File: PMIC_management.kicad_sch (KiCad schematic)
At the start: 25 parts, among them SW1 SW_Push, SW2 SW_Push, U3 RK809-2, Y2 32.768Khz

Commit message: updated Reference, and PCB
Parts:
- BT1: footprint (none) -> TestPoint:TestPoint_2Pads_Pitch5.08mm_Drill1.3mm
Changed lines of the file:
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@@
       (effects (font (size 1.27 1.27)) (justify left))
     )
-    (property "Footprint" "" (at 237.49 44.196 90)
+    (property "Footprint" "TestPoint:TestPoint_2Pads_Pitch5.08mm_Drill1.3mm" (at 237.49 44.196 90)
       (effects (font (size 1.27 1.27)) hide)
     )

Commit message: updated LCSC selection of capacitors
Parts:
- C43, C49: value 100nF X5R 16V -> 100nF X5R 6.3V; footprint Capacitor_SMD:C_0402_1005Metric -> Capacitor_SMD:C_0201_0603Metric; LCSC (none) -> C76934; Model (none) -> GRM033R61A104KE15D; Vendor (none) -> muRata(村田)
- C44, C45: value 22uF 50V C0G -> 22pF 50V C0G; footprint Capacitor_SMD:C_0402_1005Metric -> Capacitor_SMD:C_0201_0603Metric; LCSC (none) -> C76924; Model (none) -> GRM0335C1H220JA01D; Vendor (none) -> muRata(村田)
- C46, C47: value 1uF 10V X5R -> 1uF X5R 6.3V; footprint Capacitor_SMD:C_0402_1005Metric -> Capacitor_SMD:C_0201_0603Metric; LCSC (none) -> C76929; Model (none) -> GRM033R60J105KEA2D; Vendor (none) -> muRata(村田)
- C48: footprint (none) -> Capacitor_SMD:C_0603_1608Metric
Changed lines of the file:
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@@
       (effects (font (size 1.27 1.27)))
     )
-    (property "Value" "22uF 50V C0G" (at 74.93 76.2 90)
-      (effects (font (size 1.27 1.27)))
-    )
-    (property "Footprint" "Capacitor_SMD:C_0402_1005Metric" (at 69.85 73.9648 0)
+    (property "Value" "22pF 50V C0G" (at 74.93 76.2 90)
+      (effects (font (size 1.27 1.27)))
+    )
+    (property "Footprint" "Capacitor_SMD:C_0201_0603Metric" (at 69.85 73.9648 0)
       (effects (font (size 1.27 1.27)) hide)
     )
     (property "Datasheet" "~" (at 66.04 74.93 0)
+      (effects (font (size 1.27 1.27)) hide)
+    )
+    (property "Description" "容值: 22pF 精度: ±5% 额定电压: 50V 材质(温度系数): C0G 材质:C0G" (at 66.04 74.93 0)
+      (effects (font (size 1.27 1.27)) hide)
+    )
+    (property "LCSC" "C76924" (at 66.04 74.93 0)
+      (effects (font (size 1.27 1.27)) hide)
+    )
+    (property "Model" "GRM0335C1H220JA01D" (at 66.04 74.93 0)
+      (effects (font (size 1.27 1.27)) hide)
+    )
+    (property "Vendor" "muRata(村田)" (at 66.04 74.93 0)
       (effects (font (size 1.27 1.27)) hide)
     )
@@
       (effects (font (size 1.27 1.27)))
     )
-    (property "Value" "22uF 50V C0G" (at 74.93 66.04 90)
-      (effects (font (size 1.27 1.27)))
-    )
-    (property "Footprint" "Capacitor_SMD:C_0402_1005Metric" (at 69.85 66.3448 0)
+    (property "Value" "22pF 50V C0G" (at 74.93 66.04 90)
+      (effects (font (size 1.27 1.27)))
+    )
+    (property "Footprint" "Capacitor_SMD:C_0201_0603Metric" (at 69.85 66.3448 0)
       (effects (font (size 1.27 1.27)) hide)
     )
     (property "Datasheet" "~" (at 66.04 67.31 0)
+      (effects (font (size 1.27 1.27)) hide)
+    )
+    (property "Description" "容值: 22pF 精度: ±5% 额定电压: 50V 材质(温度系数): C0G 材质:C0G" (at 66.04 67.31 0)
+      (effects (font (size 1.27 1.27)) hide)
+    )
+    (property "LCSC" "C76924" (at 66.04 67.31 0)
+      (effects (font (size 1.27 1.27)) hide)
+    )
+    (property "Model" "GRM0335C1H220JA01D" (at 66.04 67.31 0)
+      (effects (font (size 1.27 1.27)) hide)
+    )
+    (property "Vendor" "muRata(村田)" (at 66.04 67.31 0)
       (effects (font (size 1.27 1.27)) hide)
     )
@@
       (effects (font (size 1.27 1.27)) (justify left))
     )
-    (property "Value" "100nF X5R 16V" (at 36.83 130.81 0)
-      (effects (font (size 1.27 1.27)) (justify left))
-    )
-    (property "Footprint" "Capacitor_SMD:C_0402_1005Metric" (at 53.0352 130.81 0)
+    (property "Value" "100nF X5R 6.3V" (at 36.83 130.81 0)
+      (effects (font (size 1.27 1.27)) (justify left))
+    )
+    (property "Footprint" "Capacitor_SMD:C_0201_0603Metric" (at 53.0352 130.81 0)
       (effects (font (size 1.27 1.27)) hide)
     )
@@
       (effects (font (size 1.27 1.27)) hide)
     )
+    (property "Description" "容值: 100nF 精度: ±10% 额定电压: 10V 材质(温度系数): X5R 材质:X5R" (at 52.07 127 0)
+      (effects (font (size 1.27 1.27)) hide)
+    )
+    (property "Model" "GRM033R61A104KE15D" (at 52.07 127 0)
+      (effects (font (size 1.27 1.27)) hide)
+    )
+    (property "Vendor" "muRata(村田)" (at 52.07 127 0)
+      (effects (font (size 1.27 1.27)) hide)
+    )
+    (property "LCSC" "C76934" (at 52.07 127 0)
+      (effects (font (size 1.27 1.27)) hide)
+    )
     (pin "1")
     (pin "2")
@@
       (effects (font (size 1.27 1.27)))
     )
-    (property "Value" "1uF 10V X5R" (at 168.91 51.3621 90)
-      (effects (font (size 1.27 1.27)))
-    )
-    (property "Footprint" "Capacitor_SMD:C_0402_1005Metric" (at 172.72 53.6448 0)
+    (property "Value" "1uF X5R 6.3V" (at 168.91 51.3621 90)
+      (effects (font (size 1.27 1.27)))
+    )
+    (property "Footprint" "Capacitor_SMD:C_0201_0603Metric" (at 172.72 53.6448 0)
       (effects (font (size 1.27 1.27)) hide)
     )
@@
       (effects (font (size 1.27 1.27)) hide)
     )
+    (property "Description" "容值: 1uF 精度: ±10% 额定电压: 6.3V 材质(温度系数): X5R 材质:X5R" (at 168.91 54.61 0)
+      (effects (font (size 1.27 1.27)) hide)
+    )
+    (property "LCSC" "C76929" (at 168.91 54.61 0)
+      (effects (font (size 1.27 1.27)) hide)
+    )
+    (property "Model" "GRM033R60J105KEA2D" (at 168.91 54.61 0)
+      (effects (font (size 1.27 1.27)) hide)
+    )
+    (property "Vendor" "muRata(村田)" (at 168.91 54.61 0)
+      (effects (font (size 1.27 1.27)) hide)
+    )
     (pin "1")
     (pin "2")
@@
       (effects (font (size 1.27 1.27)) (justify left))
     )
-    (property "Footprint" "" (at 178.7652 107.95 0)
+    (property "Footprint" "Capacitor_SMD:C_0603_1608Metric" (at 178.7652 107.95 0)
       (effects (font (size 1.27 1.27)) hide)
     )
@@
       (effects (font (size 1.27 1.27)) (justify right))
     )
-    (property "Value" "100nF X5R 16V" (at 238.76 132.08 90)
-      (effects (font (size 1.27 1.27)) (justify right))
-    )
-    (property "Footprint" "Capacitor_SMD:C_0402_1005Metric" (at 240.03 133.6548 0)
+    (property "Value" "100nF X5R 6.3V" (at 238.76 132.08 90)
+      (effects (font (size 1.27 1.27)) (justify right))
+    )
+    (property "Footprint" "Capacitor_SMD:C_0201_0603Metric" (at 240.03 133.6548 0)
       (effects (font (size 1.27 1.27)) hide)
     )
@@
       (effects (font (size 1.27 1.27)) hide)
     )
+    (property "Description" "容值: 100nF 精度: ±10% 额定电压: 10V 材质(温度系数): X5R 材质:X5R" (at 236.22 134.62 0)
+      (effects (font (size 1.27 1.27)) hide)
+    )
+    (property "Model" "GRM033R61A104KE15D" (at 236.22 134.62 0)
+      (effects (font (size 1.27 1.27)) hide)
+    )
+    (property "Vendor" "muRata(村田)" (at 236.22 134.62 0)
+      (effects (font (size 1.27 1.27)) hide)
+    )
+    (property "LCSC" "C76934" (at 236.22 134.62 0)
+      (effects (font (size 1.27 1.27)) hide)
+    )
     (pin "1")
     (pin "2")
@@
       (effects (font (size 1.27 1.27)))
     )
-    (property "Value" "1uF 10V X5R" (at 86.36 52.07 90)
-      (effects (font (size 1.27 1.27)))
-    )
-    (property "Footprint" "Capacitor_SMD:C_0402_1005Metric" (at 82.55 52.3748 0)
+    (property "Value" "1uF X5R 6.3V" (at 86.36 52.07 90)
+      (effects (font (size 1.27 1.27)))
+    )
+    (property "Footprint" "Capacitor_SMD:C_0201_0603Metric" (at 82.55 52.3748 0)
       (effects (font (size 1.27 1.27)) hide)
     )
@@
       (effects (font (size 1.27 1.27)) hide)
     )
+    (property "Description" "容值: 1uF 精度: ±10% 额定电压: 6.3V 材质(温度系数): X5R 材质:X5R" (at 78.74 53.34 0)
+      (effects (font (size 1.27 1.27)) hide)
+    )
+    (property "LCSC" "C76929" (at 78.74 53.34 0)
+      (effects (font (size 1.27 1.27)) hide)
+    )
+    (property "Model" "GRM033R60J105KEA2D" (at 78.74 53.34 0)
+      (effects (font (size 1.27 1.27)) hide)
+    )
+    (property "Vendor" "muRata(村田)" (at 78.74 53.34 0)
+      (effects (font (size 1.27 1.27)) hide)
+    )

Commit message: updated foorprints
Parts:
- D13: value ESD545IN -> ESD 3.3V; footprint Diode_SMD:D_0402_1005Metric -> Diode_SMD:Nexperia_DSN0603-2_0.6x0.3mm_P0.4mm; LCSC (none) -> C172400; Model (none) -> LESD11D3.3CT5G; Vendor (none) -> LRC(乐山无线电)
- D14, D15: value ESD545IN -> ESD 5.0V; footprint Diode_SMD:D_0402_1005Metric -> Diode_SMD:Nexperia_DSN0603-2_0.6x0.3mm_P0.4mm; LCSC (none) -> C172403; Model (none) -> LESD11LL5.0CT5G; Vendor (none) -> LRC(乐山无线电)
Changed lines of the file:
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@@
     (stroke (width 0) (type default))
+  )
+  (text_box "PWR_ON: Power on key input, active low, internal 17k resistor pull high\nto VCC_RTC"
+    (at 134.62 120.65 0) (size 38.1 8.89)
+    (stroke (width 0) (type dash_dot) (color 194 194 0 1))
+    (fill (type none))
+    (effects (font (size 1.27 1.27) (color 194 194 0 1)) (justify left top))
   )
   (text "还需要考虑充电/保护电路" (at 210.82 22.86 0)
@@
       (effects (font (size 1.27 1.27)) (justify right))
     )
-    (property "Value" "ESD545IN" (at 237.49 121.92 0)
-      (effects (font (size 1.27 1.27)) (justify right))
-    )
-    (property "Footprint" "Diode_SMD:D_0402_1005Metric" (at 236.22 124.46 0)
-      (effects (font (size 1.27 1.27)) hide)
-    )
-    (property "Datasheet" "https://www.onsemi.com/pub/Collateral/ESD9B-D.PDF" (at 236.22 124.46 0)
+    (property "Value" "ESD 5.0V" (at 237.49 121.92 0)
+      (effects (font (size 1.27 1.27)) (justify right))
+    )
+    (property "Footprint" "Diode_SMD:Nexperia_DSN0603-2_0.6x0.3mm_P0.4mm" (at 236.22 124.46 0)
+      (effects (font (size 1.27 1.27)) hide)
+    )
+    (property "Datasheet" "" (at 236.22 124.46 0)
+      (effects (font (size 1.27 1.27)) hide)
+    )
+    (property "Description" "极性: 双向 反向截止电压(Vrwm): 5V 击穿电压(VBR): 6V 峰值脉冲电流(Ipp)@8/20us: 4A 钳位电压(Vc)@Ipp: 20V" (at 236.22 124.46 0)
+      (effects (font (size 1.27 1.27)) hide)
+    )
+    (property "LCSC" "C172403" (at 236.22 124.46 0)
+      (effects (font (size 1.27 1.27)) hide)
+    )
+    (property "Model" "LESD11LL5.0CT5G" (at 236.22 124.46 0)
+      (effects (font (size 1.27 1.27)) hide)
+    )
+    (property "Vendor" "LRC(乐山无线电)" (at 236.22 124.46 0)
       (effects (font (size 1.27 1.27)) hide)
     )
@@
       (effects (font (size 1.27 1.27)) (justify right))
     )
-    (property "Value" "ESD545IN" (at 267.97 44.45 90)
-      (effects (font (size 1.27 1.27)) (justify right))
-    )
-    (property "Footprint" "Diode_SMD:D_0402_1005Metric" (at 265.43 43.18 0)
-      (effects (font (size 1.27 1.27)) hide)
-    )
-    (property "Datasheet" "https://www.onsemi.com/pub/Collateral/ESD9B-D.PDF" (at 265.43 43.18 0)
+    (property "Value" "ESD 5.0V" (at 267.97 44.45 90)
+      (effects (font (size 1.27 1.27)) (justify right))
+    )
+    (property "Footprint" "Diode_SMD:Nexperia_DSN0603-2_0.6x0.3mm_P0.4mm" (at 265.43 43.18 0)
+      (effects (font (size 1.27 1.27)) hide)
+    )
+    (property "Datasheet" "" (at 265.43 43.18 0)
+      (effects (font (size 1.27 1.27)) hide)
+    )
+    (property "Description" "极性: 双向 反向截止电压(Vrwm): 5V 击穿电压(VBR): 6V 峰值脉冲电流(Ipp)@8/20us: 4A 钳位电压(Vc)@Ipp: 20V" (at 265.43 43.18 0)
+      (effects (font (size 1.27 1.27)) hide)
+    )
+    (property "LCSC" "C172403" (at 265.43 43.18 0)
+      (effects (font (size 1.27 1.27)) hide)
+    )
+    (property "Model" "LESD11LL5.0CT5G" (at 265.43 43.18 0)
+      (effects (font (size 1.27 1.27)) hide)
+    )
+    (property "Vendor" "LRC(乐山无线电)" (at 265.43 43.18 0)
       (effects (font (size 1.27 1.27)) hide)
     )
@@
       (effects (font (size 1.27 1.27)) (justify right))
     )
-    (property "Value" "ESD545IN" (at 69.85 128.27 90)
-      (effects (font (size 1.27 1.27)) (justify right))
-    )
-    (property "Footprint" "Diode_SMD:D_0402_1005Metric" (at 67.31 127 0)
-      (effects (font (size 1.27 1.27)) hide)
-    )
-    (property "Datasheet" "https://www.onsemi.com/pub/Collateral/ESD9B-D.PDF" (at 67.31 127 0)
-      (effects (font (size 1.27 1.27)) hide)
-    )
+    (property "Value" "ESD 3.3V" (at 69.85 128.27 90)
+      (effects (font (size 1.27 1.27)) (justify right))
+    )
+    (property "Footprint" "Diode_SMD:Nexperia_DSN0603-2_0.6x0.3mm_P0.4mm" (at 67.31 127 0)
+      (effects (font (size 1.27 1.27)) hide)
+    )
+    (property "Datasheet" "" (at 67.31 127 0)
+      (effects (font (size 1.27 1.27)) hide)
+    )
+    (property "Description" "极性: 双向 反向截止电压(Vrwm): 3.3V 击穿电压(VBR): 5V 峰值脉冲电流(Ipp)@8/20us: 6A 钳位电压" (at 67.31 127 0)
+      (effects (font (size 1.27 1.27)) hide)
+    )
+    (property "LCSC" "C172400" (at 67.31 127 0)
+      (effects (font (size 1.27 1.27)) hide)
+    )
+    (property "Model" "LESD11D3.3CT5G" (at 67.31 127 0)
+      (effects (font (size 1.27 1.27)) hide)
+    )
+    (property "Vendor" "LRC(乐山无线电)" (at 67.31 127 0)
+      (effects (font (size 1.27 1.27)) hide)
+    )

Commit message: layout SoC Power and DDR capacitors
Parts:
- C43, C49: LCSC C76934 -> C76928; Model GRM033R61A104KE15D -> GRM033R60J104KE19D
- C46, C47: footprint Capacitor_SMD:C_0201_0603Metric -> Capacitor_SMD:C_0402_1005Metric; LCSC C76929 -> C15684; Model GRM033R60J105KEA2D -> GRM155R60J105KE19D
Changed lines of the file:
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@@
       (effects (font (size 1.27 1.27)) hide)
     )
-    (property "Description" "容值: 100nF 精度: ±10% 额定电压: 10V 材质(温度系数): X5R 材质:X5R" (at 52.07 127 0)
-      (effects (font (size 1.27 1.27)) hide)
-    )
-    (property "Model" "GRM033R61A104KE15D" (at 52.07 127 0)
+    (property "Description" "容值: 100nF 精度: ±10% 额定电压: 6.3V 材质(温度系数): X5R 材质:X5R" (at 52.07 127 0)
+      (effects (font (size 1.27 1.27)) hide)
+    )
+    (property "Model" "GRM033R60J104KE19D" (at 52.07 127 0)
       (effects (font (size 1.27 1.27)) hide)
     )
@@
       (effects (font (size 1.27 1.27)) hide)
     )
-    (property "LCSC" "C76934" (at 52.07 127 0)
+    (property "LCSC" "C76928" (at 52.07 127 0)
       (effects (font (size 1.27 1.27)) hide)
     )
@@
       (effects (font (size 1.27 1.27)))
     )
-    (property "Footprint" "Capacitor_SMD:C_0201_0603Metric" (at 172.72 53.6448 0)
+    (property "Footprint" "Capacitor_SMD:C_0402_1005Metric" (at 172.72 53.6448 0)
       (effects (font (size 1.27 1.27)) hide)
     )
@@
       (effects (font (size 1.27 1.27)) hide)
     )
-    (property "LCSC" "C76929" (at 168.91 54.61 0)
-      (effects (font (size 1.27 1.27)) hide)
-    )
-    (property "Model" "GRM033R60J105KEA2D" (at 168.91 54.61 0)
+    (property "LCSC" "C15684" (at 168.91 54.61 0)
+      (effects (font (size 1.27 1.27)) hide)
+    )
+    (property "Model" "GRM155R60J105KE19D" (at 168.91 54.61 0)
       (effects (font (size 1.27 1.27)) hide)
     )
@@
       (effects (font (size 1.27 1.27)) hide)
     )
-    (property "Description" "容值: 100nF 精度: ±10% 额定电压: 10V 材质(温度系数): X5R 材质:X5R" (at 236.22 134.62 0)
-      (effects (font (size 1.27 1.27)) hide)
-    )
-    (property "Model" "GRM033R61A104KE15D" (at 236.22 134.62 0)
+    (property "Description" "容值: 100nF 精度: ±10% 额定电压: 6.3V 材质(温度系数): X5R 材质:X5R" (at 236.22 134.62 0)
+      (effects (font (size 1.27 1.27)) hide)
+    )
+    (property "Model" "GRM033R60J104KE19D" (at 236.22 134.62 0)
       (effects (font (size 1.27 1.27)) hide)
     )
@@
       (effects (font (size 1.27 1.27)) hide)
     )
-    (property "LCSC" "C76934" (at 236.22 134.62 0)
+    (property "LCSC" "C76928" (at 236.22 134.62 0)
       (effects (font (size 1.27 1.27)) hide)
     )
@@
       (effects (font (size 1.27 1.27)))
     )
-    (property "Footprint" "Capacitor_SMD:C_0201_0603Metric" (at 82.55 52.3748 0)
+    (property "Footprint" "Capacitor_SMD:C_0402_1005Metric" (at 82.55 52.3748 0)
       (effects (font (size 1.27 1.27)) hide)
     )
@@
       (effects (font (size 1.27 1.27)) hide)
     )
-    (property "LCSC" "C76929" (at 78.74 53.34 0)
-      (effects (font (size 1.27 1.27)) hide)
-    )
-    (property "Model" "GRM033R60J105KEA2D" (at 78.74 53.34 0)
-      (effects (font (size 1.27 1.27)) hide)
-    )
+    (property "LCSC" "C15684" (at 78.74 53.34 0)
+      (effects (font (size 1.27 1.27)) hide)
+    )
+    (property "Model" "GRM155R60J105KE19D" (at 78.74 53.34 0)
+      (effects (font (size 1.27 1.27)) hide)
+    )

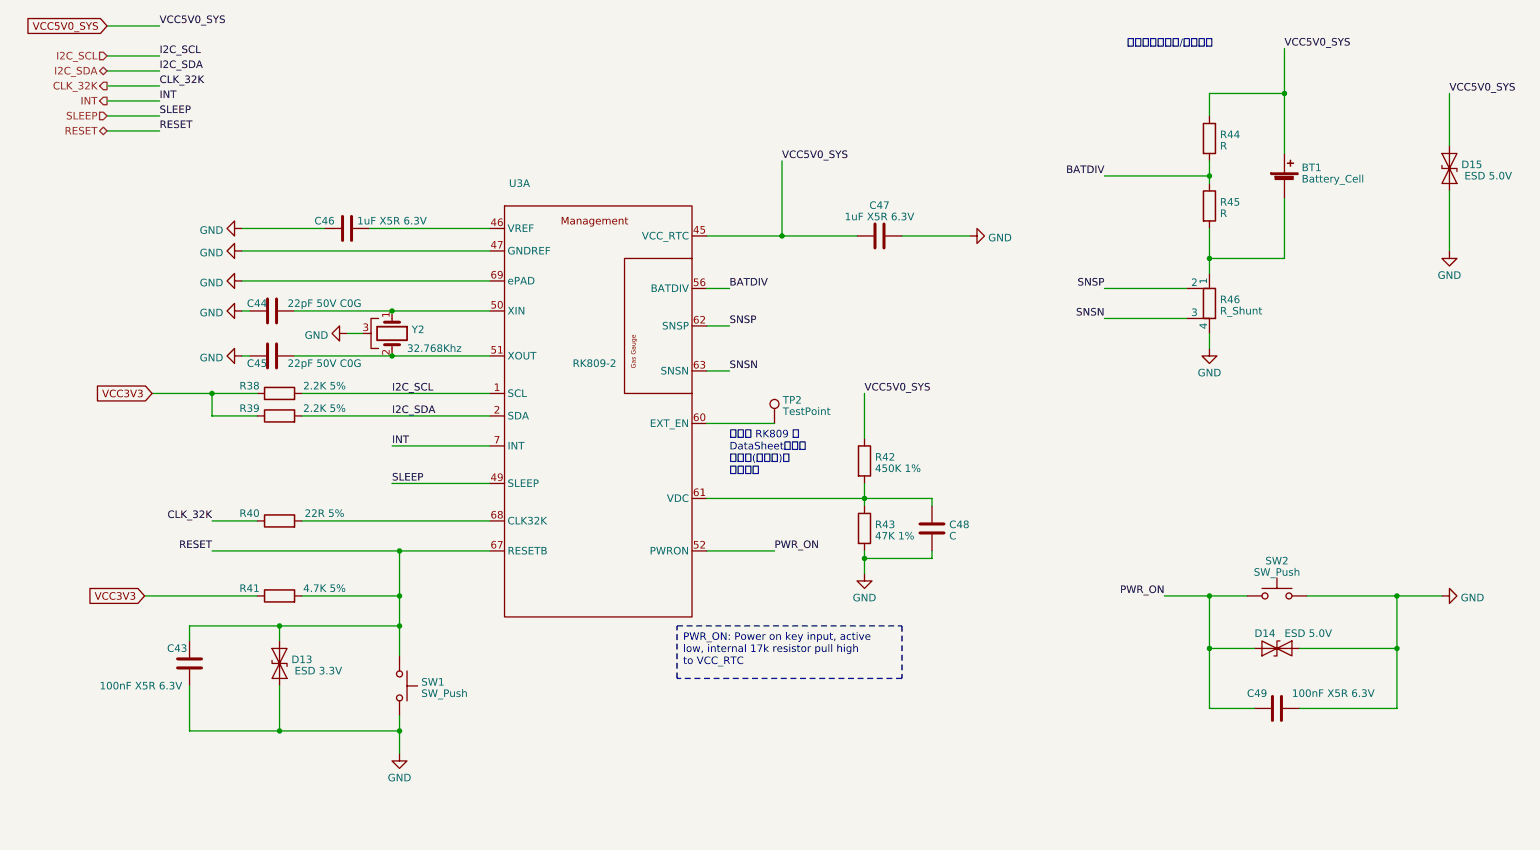
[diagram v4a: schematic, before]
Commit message: updated Resistors
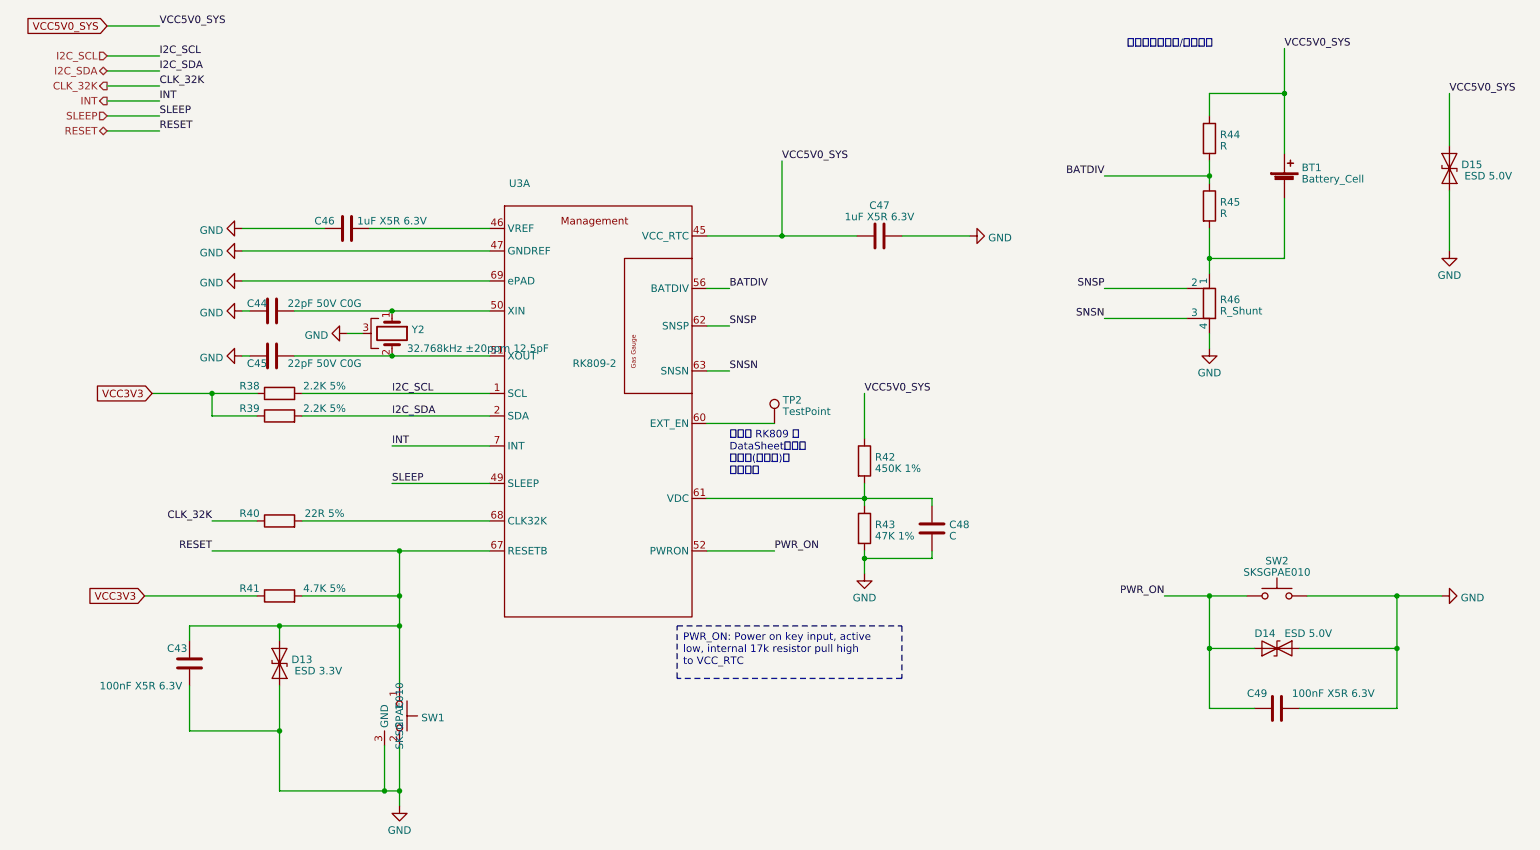
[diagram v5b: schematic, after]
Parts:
- removed SW1: SW_Push, symbol Switch:SW_Push
- added SW1: SKSGPAE010, Leaf_Button_Switch_SMD:SW_SPST_ALPS_SKSG_3.9x2.7mm, symbol Leaf_Switch:SW_Push_SPST
- C43: footprint Capacitor_SMD:C_0201_0603Metric -> Capacitor_SMD:C_0402_1005Metric; LCSC C76928 -> C161163; Model GRM033R60J104KE19D -> GCM155R71A104KA55D
- R38, R39: LCSC (none) -> C966701; Model (none) -> CQ02WGJ0222TCE; Vendor (none) -> UNI-ROYAL(厚声)
- R40: LCSC (none) -> C59651; Model (none) -> 0402WGF221JTCE; Vendor (none) -> UNI-ROYAL(厚声)
- R41: LCSC (none) -> C25940; Model (none) -> 0402WGJ0472TCE; Vendor (none) -> UNI-ROYAL(厚声)
- SW2: value SW_Push -> SKSGPAE010; footprint (none) -> Leaf_Button_Switch_SMD:SW_SPST_ALPS_SKSG_3.9x2.7mm; LCSC (none) -> C125045; Model (none) -> SKSGPAE010; Vendor (none) -> ALPSALPINE(阿尔卑斯阿尔
- Y2: value 32.768Khz -> 32.768kHz ±20ppm 12.5pF; footprint (none) -> Crystal:Crystal_SMD_3215-2Pin_3.2x1.5mm; LCSC (none) -> C32346; Model (none) -> Q13FC1350000400; Vendor (none) -> EPSON(爱普生)
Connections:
- net GND: now also SW1.2, SW1.3 (GND)
- net RESET: now also SW1.1
